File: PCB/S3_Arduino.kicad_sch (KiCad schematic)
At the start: 29 parts

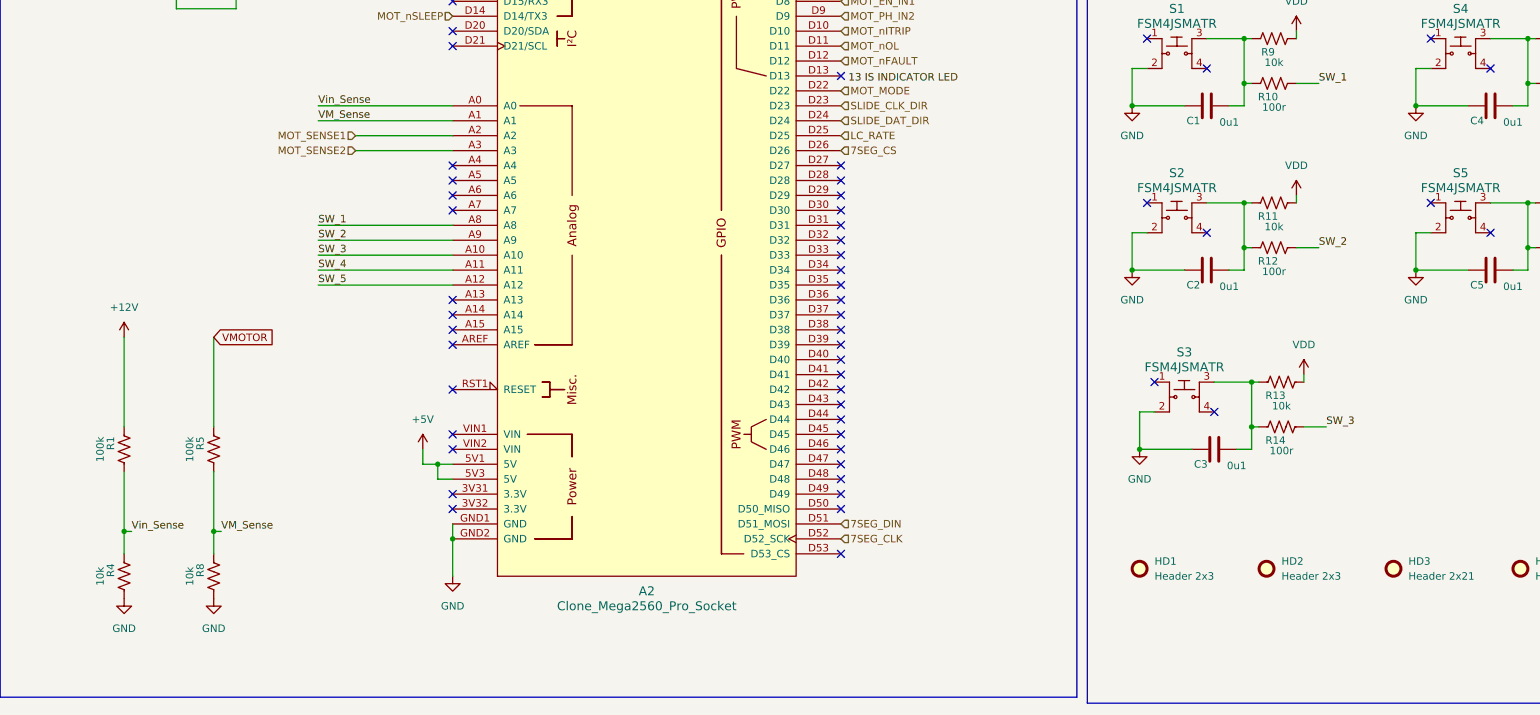
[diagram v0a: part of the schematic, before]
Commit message: Update PCB to seperate ground symbols apporiately. Modify board to sepearte ground path for motor current and all other devices. Add filtering for slide power, hopefully reduce bownout or other issue.
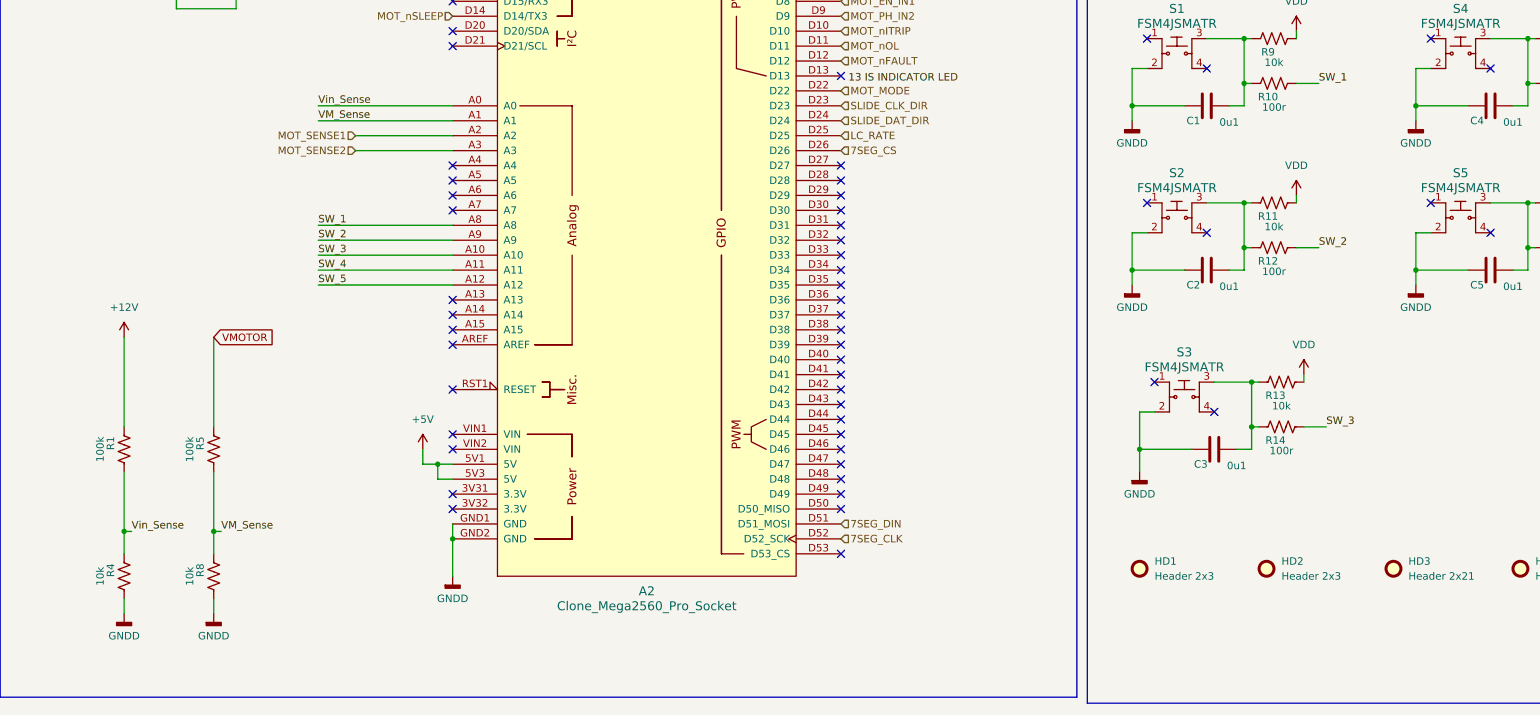
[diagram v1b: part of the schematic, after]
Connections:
- net GND renamed GNDD

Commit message: Starting work to put arduino chip directly onboard
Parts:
- added U3: ATmega2560-16A, Package_QFP:TQFP-100_14x14mm_P0.5mm, symbol MCU_Microchip_ATmega:ATmega2560-16A
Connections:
- new net: U3.10 (VCC), U3.31 (VCC), U3.61 (VCC), U3.80 (VCC)
- new net: U3.11 (GND), U3.32 (GND), U3.62 (GND), U3.81 (GND), U3.99 (GND)
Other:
- note added: "Arduno MEGA is 5V"
- note removed: "Arduno MEGA is 5V, Other newer variants of the Mega is 3.3v IO"
- moved on the sheet: A2, C1, C2, C3, C4, C5, HD1, HD2, HD3, HD4, R1, R10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

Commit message: WIP Adding adudino onboard, so far copying pro mega
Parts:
- added C25, C26, C32, C33, C34, C35: C, symbol Device:C
- added C27, C28, C29, C30, C31: 0u1, Capacitor_SMD:C_0603_1608Metric, symbol Device:C
- added F1: Polyfuse, symbol Device:Polyfuse
- added R38, R41, R42, R43: R_US, symbol Device:R_US
- added R39: 10k, Resistor_SMD:R_0603_1608Metric, symbol Device:R_US
- added R40: 100r, Resistor_SMD:R_0603_1608Metric, symbol Device:R_US
- added S6: FSM4JSMATR, digikey-footprints:Switch_Tactile_SMD_6x6mm, symbol dk_Tactile-Switches:FSM4JSMATR
- added U4: CH340G, Package_SO:SOIC-16_3.9x9.9mm_P1.27mm, symbol Interface_USB:CH340G
- added Y1, Y2: Crystal, symbol Device:Crystal
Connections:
- net +5V: now also F1.2, R39.2
- net GNDD: now also U3.11 (GND), U3.32 (GND), U3.62 (GND), U3.81 (GND), U3.99 (GND), C25.1, C26.1, C27.1, C28.1, C29.1, C30.1, C33.2, C34.1, C35.1, S6.2, U4.1 (GND)
- net ARDUINO_VCC: now reaches U3.10 (VCC), U3.31 (VCC), U3.61 (VCC), U3.80 (VCC)
- net ARDUINO_VCC: now also U3.100 (AVCC), C28.2, C29.2, C30.2, F1.1, R42.1, U4.16 (VCC)
- net D17: now reaches U3.12 (PH0)
- net D16: now reaches U3.13 (PH1)
- net D6: now reaches U3.15 (PH3)
- net D7: now reaches U3.16 (PH4)
- net D8: now reaches U3.17 (PH5)
- net D9: now reaches U3.18 (PH6)
- net D53: now reaches U3.19 (PB0)
- net D0: now reaches U3.2 (PE0)
- net D0: now also U4.2 (TXD)
- net D52: now reaches U3.20 (PB1)
- net D51: now reaches U3.21 (PB2)
- net D50: now reaches U3.22 (PB3)
- net D10: now reaches U3.23 (PB4)
- net D11: now reaches U3.24 (PB5)
- net D12: now reaches U3.25 (PB6)
- net D13: now reaches U3.26 (PB7)
- net D1: now reaches U3.3 (PE1)
- net D1: now also U4.3 (RXD)
- net SW_RESET: now reaches U3.30 (~{RESET})
- net SW_RESET: now also R40.2
- net at U3.33 (XTAL2): now also R38.1
- net at U3.34 (XTAL1): now also C26.2, R41.1, Y1.1
- net D49: now reaches U3.35 (PL0)
- net D48: now reaches U3.36 (PL1)
- net D47: now reaches U3.37 (PL2)
- net D46: now reaches U3.38 (PL3)
- net D45: now reaches U3.39 (PL4)
- net D44: now reaches U3.40 (PL5)
- net D43: now reaches U3.41 (PL6)
- net D42: now reaches U3.42 (PL7)
- net D21: now reaches U3.43 (PD0)
- net D20: now reaches U3.44 (PD1)
- net D19: now reaches U3.45 (PD2)
- net D18: now reaches U3.46 (PD3)
- net D5: now reaches U3.5 (PE3)
- net D38: now reaches U3.50 (PD7)
- net D41: now reaches U3.51 (PG0)
- net D40: now reaches U3.52 (PG1)
- net D37: now reaches U3.53 (PC0)
- net D36: now reaches U3.54 (PC1)
- net D35: now reaches U3.55 (PC2)
- net D34: now reaches U3.56 (PC3)
- net D33: now reaches U3.57 (PC4)
- net D32: now reaches U3.58 (PC5)
- net D31: now reaches U3.59 (PC6)
- net D2: now reaches U3.6 (PE4)
- net D30: now reaches U3.60 (PC7)
- net D15: now reaches U3.63 (PJ0)
- net D14: now reaches U3.64 (PJ1)
- net D3: now reaches U3.7 (PE5)
- net D39: now reaches U3.70 (PG2)
- net A15: now reaches U3.82 (PK7)
- net A14: now reaches U3.83 (PK6)
- net A13: now reaches U3.84 (PK5)
- net A12: now reaches U3.85 (PK4)
- net A11: now reaches U3.86 (PK3)
- net A10: now reaches U3.87 (PK2)
- net A9: now reaches U3.88 (PK1)
- net A8: now reaches U3.89 (PK0)
- net at U3.98 (AREF): now also C31.2
- new net: C35.2, R43.1, U4.8 (XO), Y2.2
- new net: C32.1, R42.2, U4.13 (~{DTR})
- new net: C33.1, U4.4 (V3)
- new net: C34.2, R43.2, U4.7 (XI), Y2.1
- new net: C27.2, R39.1, R40.1, S6.3
- new net: C25.2, R38.2, R41.2, Y1.2
- new net GNDA: C31.1
- new net RESET: C32.2
- no-connect marks 65 -> 90
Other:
- note added: "Internal reference voltages of nominally 1.1V, 2.56V or AVCC are provided On-chip. The voltage reference may be externally decoupled at the AREF pin by a capacitor for better noise performance."
- note added: "PG5 ( OC0B ) | D4 (PWM) PE0 ( RXD0/PCINT8 ) | D0 (RX0) PE1 ( TXD0 ) | D1 (TX0) PE2 ( XCK0/AIN0 ) | x PE3 ( OC3A/AIN1 ) | D5 (PWM) PE4 ( OC3B/INT4 ) | D2 (PWM) PE5 ( OC3C/INT5 ) | D3 (PWM) PE6 ( T3/INT6 ) | x PE7 ( CLKO/ICP3/INT7 ) | x VCC | VCC GND | GND PH0 ( RXD2 ) | D17 (RX2) PH1 ( TXD2 ) | D16 (TX2) PH2 ( XCK2 ) | x PH3 ( OC4A ) | D6 (PWM) PH4 ( OC4B ) | D7 (PWM) PH5 ( OC4C ) | D8 (PWM) PH6 (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"
- moved on the sheet: A2, R1, R4, R5, R8, U3

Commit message: Schematic bit done for adding arduino, improved motor maybe a bit by adding caps, improved slide a bit by adding protection and more caps
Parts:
- removed A2: Clone_Mega2560_Pro_Socket, AMX_Logo:Clone_Mega2560_Pro_Socket, symbol arduino-library:Clone_Mega2560_Pro_Socket
- removed C1, C2, C3, C4, C5: 0u1, Capacitor_SMD:C_0603_1608Metric, symbol Device:C
- removed C32, C33: C, symbol Device:C
- removed HD1, HD2: Header 2x3, AMX_Logo:Dummy_Header_2x3, symbol Mechanical:Fiducial
- removed HD3: Header 2x21, AMX_Logo:Dummy_Header_2x21, symbol Mechanical:Fiducial
- removed HD4: Header 2x16, AMX_Logo:Dummy_Header_2x16, symbol Mechanical:Fiducial
- removed R10, R12, R14, R16, R18: 100r, Resistor_SMD:R_0603_1608Metric, symbol Device:R_US
- removed R11, R13, R15, R17, R9: 10k, Resistor_SMD:R_0603_1608Metric, symbol Device:R_US
- removed R41, R43: R_US, symbol Device:R_US
- removed S1, S2, S3, S4, S5: FSM4JSMATR, digikey-footprints:Switch_Tactile_SMD_6x6mm, symbol dk_Tactile-Switches:FSM4JSMATR
- added C36, C37, C38: 0u1, Capacitor_SMD:C_0603_1608Metric, symbol Device:C
- added D13, D17, D18, D19, D20: GRN, LED_SMD:LED_0603_1608Metric, symbol MMTK-rescue:LED-Device-MMTK-rescue
- added D14: RED, LED_SMD:LED_0603_1608Metric, symbol MMTK-rescue:LED-Device-MMTK-rescue
- added D2: MBR0560, Diode_SMD:D_SOD-123, symbol Diode:MBR0560
- added D4: 5V Zener, Diode_SMD:D_SOD-523, symbol Diode:ESD5Zxx
- added F2: Polyfuse, symbol Device:Polyfuse
- added J4: USB_C_Receptacle_USB2.0_16P, symbol Connector:USB_C_Receptacle_USB2.0_16P
- added R44, R45: R_US, symbol Device:R_US
- added R46, R47: 2K, symbol Device:R_US
- added R48: 5K1, symbol Device:R_US
- added R56, R57, R58, R59: 1K, Resistor_SMD:R_0603_1608Metric, symbol MMTK-rescue:R_US-Device-MMTK-rescue
- added U5: USBLC6-2SC6, Package_TO_SOT_SMD:SOT-23-6, symbol Power_Protection:USBLC6-2SC6
- C25, C26, C34, C35: value C -> 33p
- R40: value 100r -> 5K1; footprint Resistor_SMD:R_0603_1608Metric -> (none)
- R42: value R_US -> 1K
- Y1: value Crystal -> HC49 16Mhz
- Y2: value Crystal -> HC49-12M
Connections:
- net D10 is gone; now on net MOT_nITRIP: U3.23 (PB4)
- net D11 is gone; now on net MOT_nOL: U3.24 (PB5)
- net D12 is gone; now on net MOT_nFAULT: U3.25 (PB6)
- net D14 is gone; now on net MOT_nSLEEP: U3.64 (PJ1)
- net D3 is gone; now on net SLIDE_CLK: U3.7 (PE5)
- net D5 is gone; now on net LC_SCK: U3.5 (PE3)
- net D51 is gone; now on net 7SEG_DIN: U3.21 (PB2)
- net D52 is gone; now on net 7SEG_CLK: U3.20 (PB1)
- net D6 is gone; now on net LC_DT: U3.15 (PH3)
- net D7 is gone; now on net MOT_DISABLE: U3.16 (PH4)
- net D8 is gone; now on net MOT_EN_IN1: U3.17 (PH5)
- net D9 is gone; now on net MOT_PH_IN2: U3.18 (PH6)
- net VM_Sense is gone; now on net A1: R5.2, R8.1
- net Vin_Sense is gone; now on net A0: R1.2, R4.1
- net +5V: now also U4.16 (VCC), C37.1, D2.1 (K), D4.1 (K), F2.1, R46.2, R47.2, U5.5 (VBUS)
- net 7SEG_CS: now also U3.74 (PA4)
- net ARDUINO_VCC: no longer R42.1, U4.16 (VCC)
- net D0: now also R44.2; no longer U4.2 (TXD)
- net D1: now also R45.2; no longer U4.3 (RXD)
- net D13: now also D17.2 (A)
- net D35: now also D20.2 (A)
- net D36: now also D19.2 (A)
- net D37: now also D18.2 (A)
- net GNDD: now also R40.2, R42.2, C36.1, C37.2, D4.2 (A), J4.A1 (GND), J4.A12 (GND), J4.B1 (GND), J4.B12 (GND), J4.S1 (SHIELD), R48.2, R56.1, R57.1, R58.1, R59.1, U5.2 (GND)
- net LC_RATE: now also U3.75 (PA3)
- net MOT_MODE: now also U3.78 (PA0)
- net MOT_SENSE1: now also U3.95 (PF2)
- net MOT_SENSE2: now also U3.94 (PF3)
- net RESET: now also C27.2, R39.1, S6.3, C38.2, D2.2 (A)
- net SLIDE_CLK_DIR: now also U3.77 (PA1)
- net SLIDE_DAT: now also U3.1 (PG5)
- net SLIDE_DAT_DIR: now also U3.76 (PA2)
- net SW_RESET: no longer R40.2
- net DTR: now reaches U4.13 (~{DTR})
- net DTR: now also R42.1, C38.1; no longer R42.2
- net at U4.4 (V3): now also C36.2
- net at U4.5 (UD+): now also U5.6 (I/O1)
- net at U4.6 (UD-): now also U5.4 (I/O2)
- net D29: now reaches U3.71 (PA7)
- net D28: now reaches U3.72 (PA6)
- net D27: now reaches U3.73 (PA5)
- net A7: now reaches U3.90 (PF7)
- net A6: now reaches U3.91 (PF6)
- net A5: now reaches U3.92 (PF5)
- net A4: now reaches U3.93 (PF4)
- net A1: now reaches U3.96 (PF1)
- net A0: now reaches U3.97 (PF0)
- net A10 renamed SW3
- net A11 renamed SW4
- net A12 renamed SW5
- net A8 renamed SW1
- net A9 renamed SW2
- net D50 renamed D50_MISO
- net D53 renamed D53_SS
- new net: D19.1 (K), R58.2
- new net: D14.1 (K), R44.1, U4.2 (TXD)
- new net: D17.1 (K), R56.2
- new net: D14.2 (A), R46.1
- new net: J4.B5 (CC2), R40.1
- new net: D13.1 (K), R45.1, U4.3 (RXD)
- new net: F2.2, J4.A4 (VBUS), J4.A9 (VBUS), J4.B4 (VBUS), J4.B9 (VBUS)
- new net: D13.2 (A), R47.1
- new net: D18.1 (K), R57.2
- new net: J4.A5 (CC1), R48.1
- new net: J4.A6 (D+), J4.B6 (D+), U5.3 (I/O2)
- new net: J4.A7 (D-), J4.B7 (D-), U5.1 (I/O1)
- new net: D20.1 (K), R59.2
- no-connect marks 90 -> 26
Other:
- note added: "NOTE FOR USBC VBUS CAN BE UP TO 20V USB NOT SUPPOSED TO POWER BOARD"
- note added: "Power and Sense"
- note added: "SPECIAL ARDUINO RESET CCT"
- note added: "USB WITH WCH340"
- note removed: "Buttons"
- moved on the sheet: C25, C26, C27, C28, C29, C30, C31, C34, C35, F1, R1, R38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
